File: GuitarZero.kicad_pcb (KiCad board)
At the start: 6 copper layers, 142 parts, among them J1 USB_A, J2 USB_B_Micro, J3 AudioJack3_SwitchT, J4 MCU_Debug, J6 Micro_SD_Card_Det_Hirose_DM3AT, SW1 SW_Push, SW2 SW_Push, SW3 SW_Push, SW4 SW_Push, SW5 SW_Push, SW6 SW_Push, U1 TPS54325, U10 FPGA_GPIO_Extra, U11 5x7 LED_matrix, U12 MCU_GPIO_Extra, U13 5x7 LED_matrix, U14 Power_Jumpers, U2 TSP54294, U3 XC7A100T-FTG256, U4 EFM32GG332, U5 S25FL127S, U6 Oscillator, U7 FPGA_JTAG_Debug, U8 PCM1754, U9 TPD_Current_Switch, Y1 Crystal_GND23

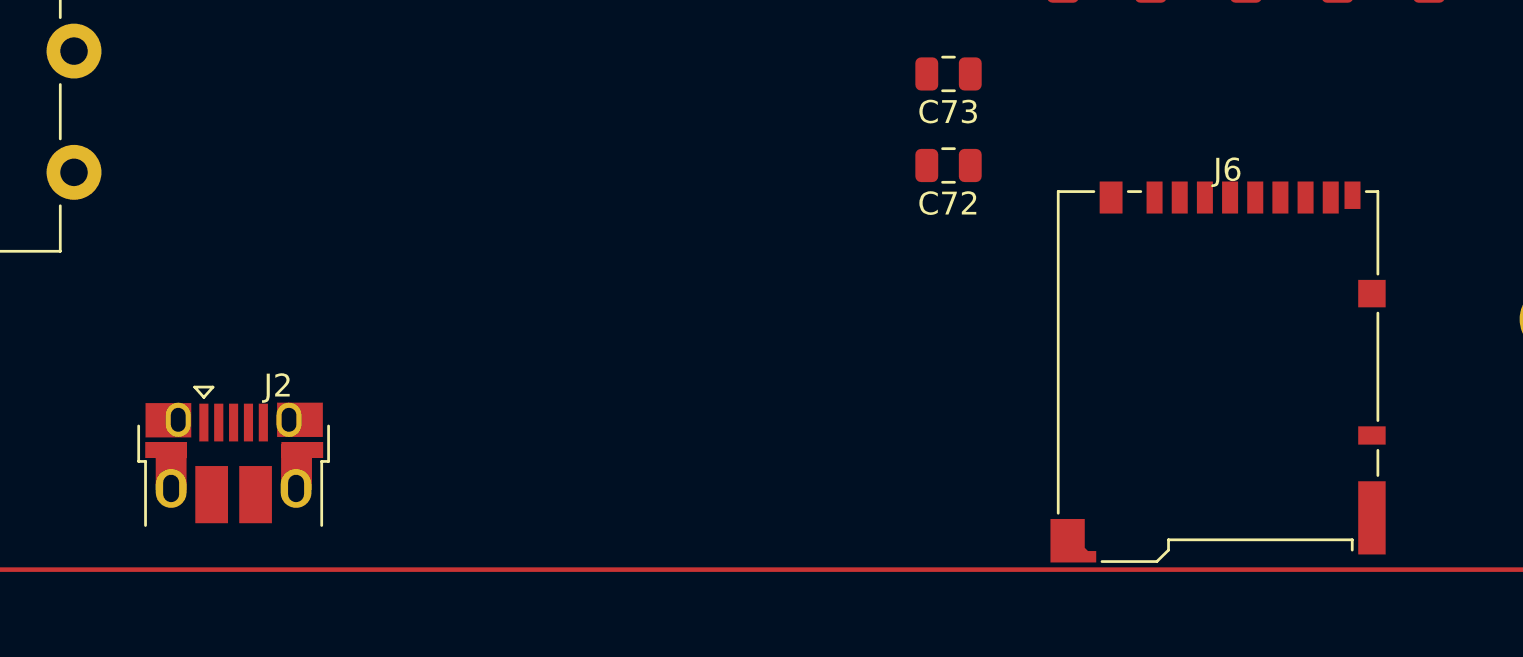
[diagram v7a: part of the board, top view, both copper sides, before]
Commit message: Added Power LED
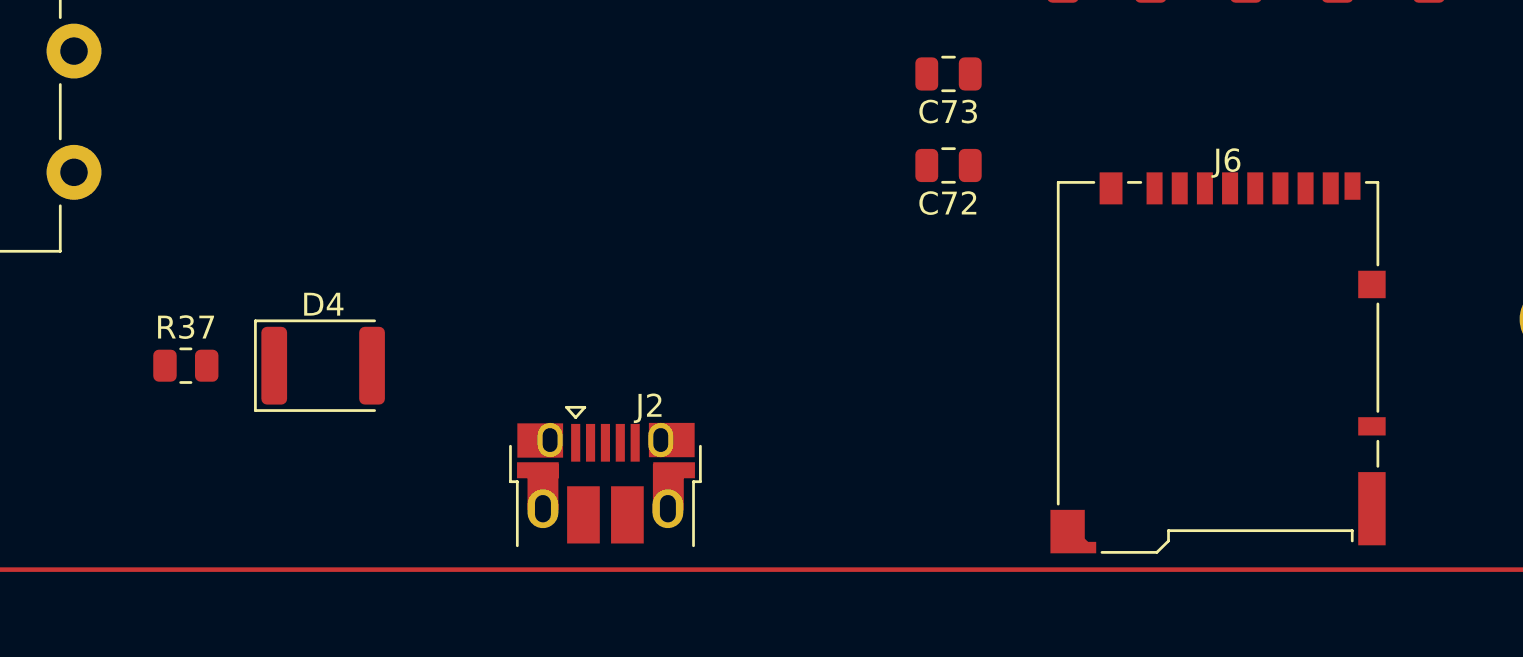
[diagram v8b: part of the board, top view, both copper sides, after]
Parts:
- added D4: LED, LED_SMD:LED_1812_4532Metric, F.Cu at (81.9, 133.8)
- added R37: 330, Resistor_SMD:R_0805_2012Metric, F.Cu at (75.9, 133.8)
- moved J2 16.3 mm to (94.2, 138.9)
- moved J6 0.40 mm to (121.0, 133.6)
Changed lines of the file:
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@@
   (net 294 "unconnected-(J6-DET_B-Pad9)")
   (net 295 "unconnected-(J6-DET_A-Pad10)")
+  (net 296 "Net-(D4-K)")
   (footprint "Inductor_SMD:L_0603_1608Metric" (layer "F.Cu")
     (at 142.87 121.805 180)
@@
   )
   (footprint "Connector_Card:microSD_HC_Hirose_DM3BT-DSF-PEJS" (layer "F.Cu")
-    (at 121 134.025)
+    (at 121 133.625)
     (descr "Micro SD, SMD, reverse on-board, right-angle, push-pull (https://www.hirose.com/product/en/download_file/key_name/DM3BT-DSF-PEJS/category/Drawing%20(2D)/doc_file_id/44097/?file_category_id=6&item_id=06090029900&is_series=)")
     (tags "Micro SD")
@@
       (polygon
         (pts
-          (xy 127.475 130)
-          (xy 128.225 130)
-          (xy 128.225 126.75)
-          (xy 127.475 126.75)
+          (xy 127.475 129.6)
+          (xy 128.225 129.6)
+          (xy 128.225 126.35)
+          (xy 127.475 126.35)
         )
       )
@@
       (polygon
         (pts
-          (xy 127.475 134.8)
-          (xy 128.225 134.8)
-          (xy 128.225 131.2)
-          (xy 127.475 131.2)
+          (xy 127.475 134.4)
+          (xy 128.225 134.4)
+          (xy 128.225 130.8)
+          (xy 127.475 130.8)
         )
       )
@@
   )
   (footprint "Connector_USB:USB_Micro-B_Amphenol_10103594-0001LF_Horizontal" (layer "F.Cu")
-    (at 78 138)
+    (at 94.25 138.885)
     (descr "Micro USB Type B 10103594-0001LF, http://cdn.amphenol-icc.com/media/wysiwyg/files/drawing/10103594.pdf")
     (tags "USB USB_B USB_micro USB_OTG")
@@
     )
   )
+  (footprint "Resistor_SMD:R_0805_2012Metric" (layer "F.Cu")
+    (at 75.8875 133.75)
+    (descr "Resistor SMD 0805 (2012 Metric), square (rectangular) end terminal, IPC_7351 nominal, (Body size source: IPC-SM-782 page 72, https://www.pcb-3d.com/wordpress/wp-content/uploads/ipc-sm-782a_amendment_1_and_2.pdf), generated with kicad-footprint-generator")
+    (tags "resistor")
+    (property "Sheetfile" "GuitarZero.kicad_sch")
+    (property "Sheetname" "")
+    (property "ki_description" "Resistor")
+    (property "ki_keywords" "R res resistor")
+    (attr smd)
+    (fp_text reference "R37" (at 0 -1.65) (layer "F.SilkS")
+        (effects (font (size 1 1) (thickness 0.15)))
+    )
+    (fp_text value "330" (at 0 1.65) (layer "F.Fab")
+        (effects (font (size 1 1) (thickness 0.15)))
+    )
+    (fp_text user "${REFERENCE}" (at 0 0) (layer "F.Fab")
+        (effects (font (size 0.5 0.5) (thickness 0.08)))
+    )
+    (fp_line (start -0.227064 -0.735) (end 0.227064 -0.735)
+      (stroke (width 0.12) (type solid)) (layer "F.SilkS"))
+    (fp_line (start -0.227064 0.735) (end 0.227064 0.735)
+      (stroke (width 0.12) (type solid)) (layer "F.SilkS"))
+    (fp_line (start -1.68 -0.95) (end 1.68 -0.95)
+      (stroke (width 0.05) (type solid)) (layer "F.CrtYd"))
+    (fp_line (start -1.68 0.95) (end -1.68 -0.95)
+      (stroke (width 0.05) (type solid)) (layer "F.CrtYd"))
+    (fp_line (start 1.68 -0.95) (end 1.68 0.95)
+      (stroke (width 0.05) (type solid)) (layer "F.CrtYd"))
+    (fp_line (start 1.68 0.95) (end -1.68 0.95)
+      (stroke (width 0.05) (type solid)) (layer "F.CrtYd"))
+    (fp_line (start -1 -0.625) (end 1 -0.625)
+      (stroke (width 0.1) (type solid)) (layer "F.Fab"))
+    (fp_line (start -1 0.625) (end -1 -0.625)
+      (stroke (width 0.1) (type solid)) (layer "F.Fab"))
+    (fp_line (start 1 -0.625) (end 1 0.625)
+      (stroke (width 0.1) (type solid)) (layer "F.Fab"))
+    (fp_line (start 1 0.625) (end -1 0.625)
+      (stroke (width 0.1) (type solid)) (layer "F.Fab"))
+    (pad "1" smd roundrect (at -0.9125 0) (size 1.025 1.4) (layers "F.Cu" "F.Paste" "F.Mask") (roundrect_rratio 0.243902)
+      (net 2 "GND") (pintype "passive"))
+    (pad "2" smd roundrect (at 0.9125 0) (size 1.025 1.4) (layers "F.Cu" "F.Paste" "F.Mask") (roundrect_rratio 0.243902)
+      (net 296 "Net-(D4-K)") (pintype "passive"))
+    (model "${KICAD6_3DMODEL_DIR}/Resistor_SMD.3dshapes/R_0805_2012Metric.wrl"
+      (offset (xyz 0 0 0))
+      (scale (xyz 1 1 1))
+      (rotate (xyz 0 0 0))
+    )
+  )
   (footprint "LED_TA20-11SRWA:LED_TA20-11SRWA" (layer "F.Cu")
     (at 103.25 61.65)
@@
       (offset (xyz 0 0 0))
       (scale (xyz 1 1 1))
+      (rotate (xyz 0 0 0))
+    )
+  )
+  (footprint "LED_SMD:LED_1812_4532Metric" (layer "F.Cu")
+    (at 81.8875 133.75)
+    (descr "LED SMD 1812 (4532 Metric), square (rectangular) end terminal, IPC_7351 nominal, (Body size source: https://www.nikhef.nl/pub/departments/mt/projects/detectorR_D/dtddice/ERJ2G.pdf), generated with kicad-footprint-generator")
+    (tags "LED")
+    (property "Sheetfile" "GuitarZero.kicad_sch")
+    (property "Sheetname" "")
+    (property "ki_description" "Light emitting diode")
+    (property "ki_keywords" "LED diode")
+    (attr smd)
+    (fp_text reference "D4" (at 0 -2.65) (layer "F.SilkS")
+        (effects (font (size 1 1) (thickness 0.15)))
+    )
+    (fp_text value "LED" (at 0 2.65) (layer "F.Fab")
+        (effects (font (size 1 1) (thickness 0.15)))
+    )
+    (fp_text user "${REFERENCE}" (at 0 0) (layer "F.Fab")
+        (effects (font (size 1 1) (thickness 0.15)))
+    )
+    (fp_line (start -2.96 -1.96) (end -2.96 1.96)
+      (stroke (width 0.12) (type solid)) (layer "F.SilkS"))
+    (fp_line (start -2.96 1.96) (end 2.25 1.96)
+      (stroke (width 0.12) (type solid)) (layer "F.SilkS"))
+    (fp_line (start 2.25 -1.96) (end -2.96 -1.96)
+      (stroke (width 0.12) (type solid)) (layer "F.SilkS"))
+    (fp_line (start -2.95 -1.95) (end 2.95 -1.95)
+      (stroke (width 0.05) (type solid)) (layer "F.CrtYd"))
+    (fp_line (start -2.95 1.95) (end -2.95 -1.95)
+      (stroke (width 0.05) (type solid)) (layer "F.CrtYd"))
+    (fp_line (start 2.95 -1.95) (end 2.95 1.95)
+      (stroke (width 0.05) (type solid)) (layer "F.CrtYd"))
+    (fp_line (start 2.95 1.95) (end -2.95 1.95)
+      (stroke (width 0.05) (type solid)) (layer "F.CrtYd"))
+    (fp_line (start -2.25 -0.8) (end -2.25 1.6)
+      (stroke (width 0.1) (type solid)) (layer "F.Fab"))
+    (fp_line (start -2.25 1.6) (end 2.25 1.6)
+      (stroke (width 0.1) (type solid)) (layer "F.Fab"))
+    (fp_line (start -1.45 -1.6) (end -2.25 -0.8)
+      (stroke (width 0.1) (type solid)) (layer "F.Fab"))
+    (fp_line (start 2.25 -1.6) (end -1.45 -1.6)
+      (stroke (width 0.1) (type solid)) (layer "F.Fab"))
+    (fp_line (start 2.25 1.6) (end 2.25 -1.6)
+      (stroke (width 0.1) (type solid)) (layer "F.Fab"))
+    (pad "1" smd roundrect (at -2.1375 0) (size 1.125 3.4) (layers "F.Cu" "F.Paste" "F.Mask") (roundrect_rratio 0.222222)
+      (net 296 "Net-(D4-K)") (pinfunction "K") (pintype "passive"))
+    (pad "2" smd roundrect (at 2.1375 0) (size 1.125 3.4) (layers "F.Cu" "F.Paste" "F.Mask") (roundrect_rratio 0.222222)
+      (net 1 "+5V") (pinfunction "A") (pintype "passive"))
+    (model "${KICAD6_3DMODEL_DIR}/LED_SMD.3dshapes/LED_1812_4532Metric.wrl"
+      (offset (xyz 0 0 0))
+      (scale (xyz 1 1 1))
